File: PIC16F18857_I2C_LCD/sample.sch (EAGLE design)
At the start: 18 parts, among them CN1 12V_IN, CN2 PIC_CN_H, SW1 10-XX, U1 XC6202P332TH, U2 PIC16F18857-I/SP, U3 AE-AQM1602A, U4 STTS751-0WB3F

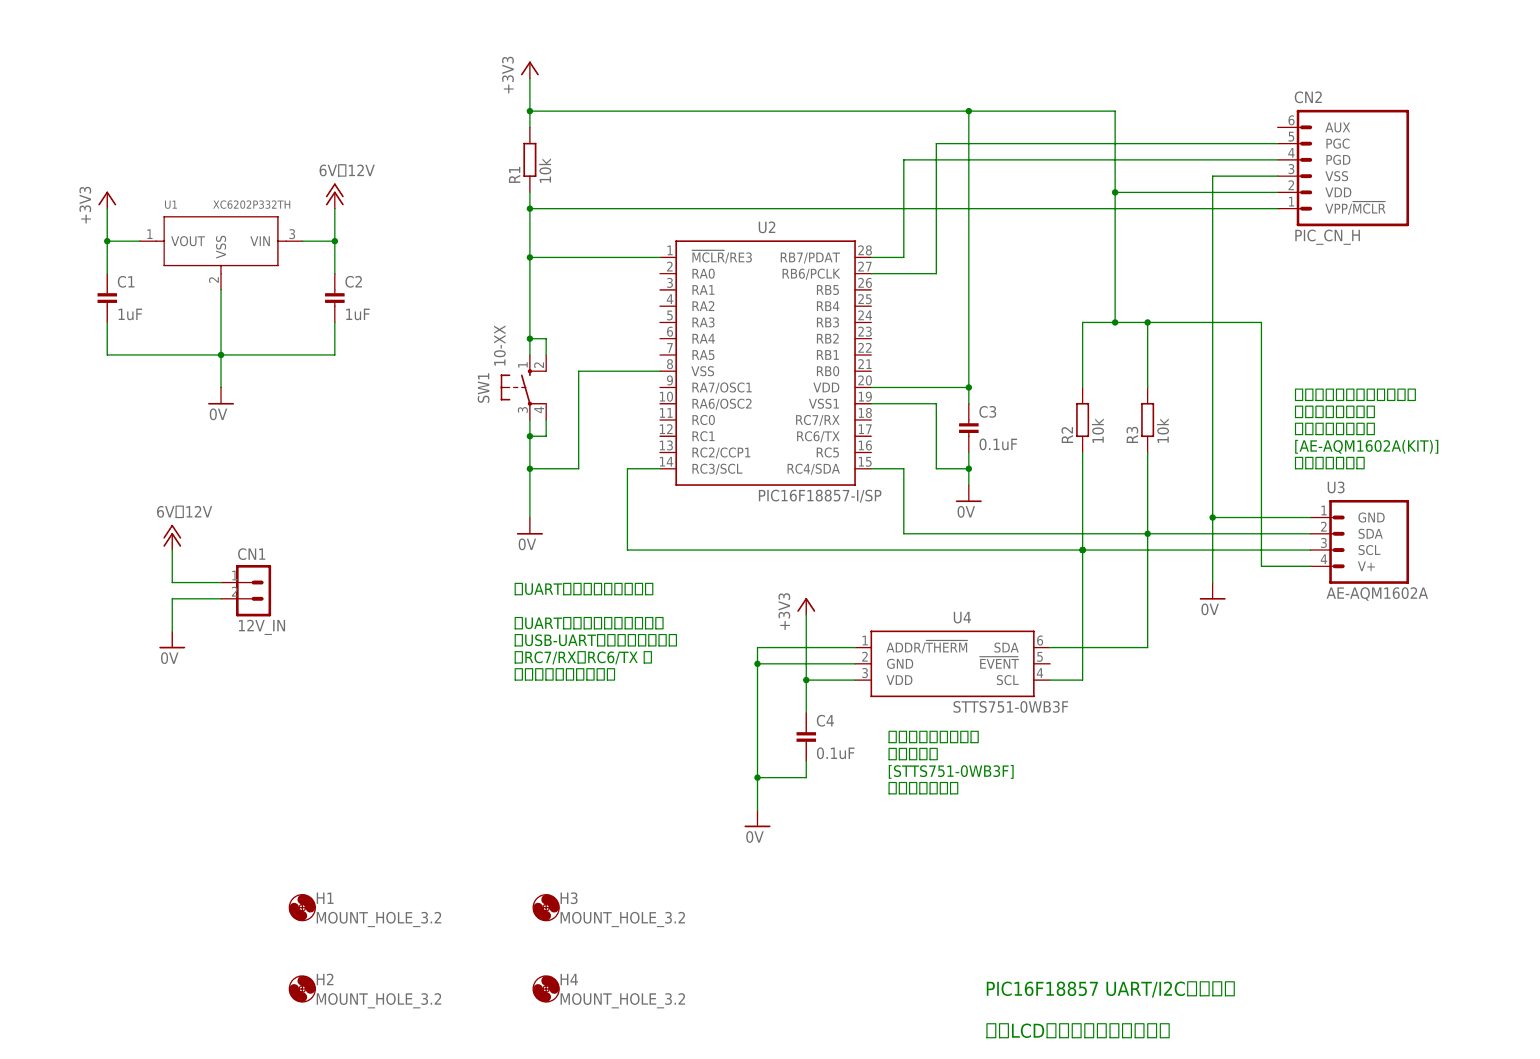
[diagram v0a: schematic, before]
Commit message: フラッシュメモリー等を回路図に追加
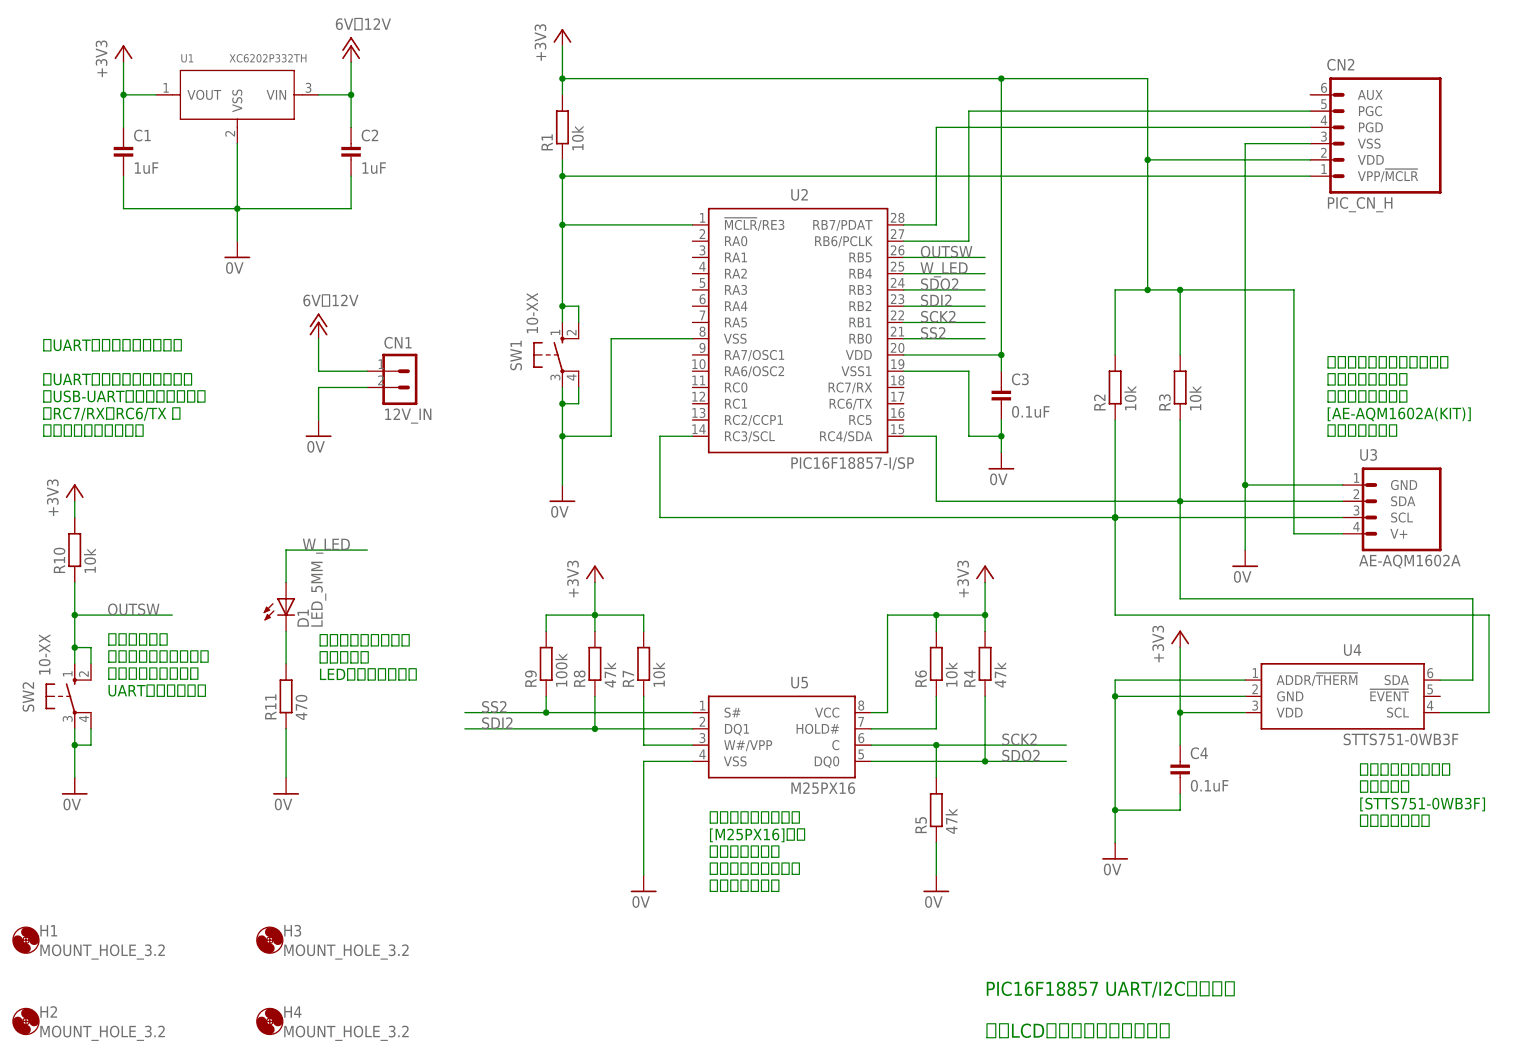
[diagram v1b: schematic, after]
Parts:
- added D1: LED_5MM, Parts:LED_5MM
- added R10, R6, R7: 10k, Parts:RESISTOR_300MIL
- added R11: 470, Parts:RESISTOR_300MIL
- added R4, R5, R8: 47k, Parts:RESISTOR_300MIL
- added R9: 100k, Parts:RESISTOR_300MIL
- added SW2: 10-XX, Parts:10-XX
- added U5: M25PX16, Parts:M25PX16
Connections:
- new net N$5: R6.1, U5.HOLD#
- new net N$7: R7.1, U5.W#/VPP
- new net N$9: D1.C, R11.2
- new net OUTSW: R10.1, SW2.S, SW2.S1, U2.RB5
- new net SCK2: R5.2, U2.RB1, U5.C
- new net SDI2: R8.1, U2.RB2, U5.DQ1
- new net SDO2: R4.1, U2.RB3, U5.DQ0
- new net SS2: R9.1, U2.RB0, U5.S#
- new net W_LED: D1.A, U2.RB4
- net +3V3: now also R10.2, R4.2, R6.2, R7.2, R8.2, R9.2, U5.VCC
- net 0V: now also R11.1, R5.1, SW2.P, SW2.P1, U5.VSS
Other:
- note added: "フラッシュメモリー [M25PX16]に、 温度センサーの 測定値が１秒ごとに 記録されます。"
- note added: "フラッシュメモリー 書込み中に LEDが点灯します。"
- note added: "ボタン押下で フラッシュメモリーに 保存されている値を UART出力します。"
- moved on the sheet: C1, C2, C3, C4, CN1, CN2, H1, H2, H3, H4, R1, R2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
